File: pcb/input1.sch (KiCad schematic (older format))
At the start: 26 parts, among them U10 74LVC245, U11 SI5351C-B, U4 PCEngineExpansion, U5 74LVC245, U6 74LVC245, U7 74LVC245, U8 74LVC245, U9 74LVC245

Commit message: Added power unit from expansion connector symbol
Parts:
- removed W1: 5V, custom_components:SMD_PAD, symbol pcehd-rescue:TestPoint-Connector
- removed W2, W3, W4, W5, W6: GND, custom_components:SMD_PAD, symbol pcehd-rescue:TestPoint-Connector
- added unit 2 of U4
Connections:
- wire segments 232 -> 233
- no-connect marks 28 -> 32
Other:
- moved on the sheet: C27, C28, C29, C30, C31, C32, D4, R6, U11, U4A, U4F

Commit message: Cleaned up schematic, moved connections to busses
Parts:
- removed C27: 47u, custom_components:SM0603_Capa_libcms, symbol pcehd-rescue:C-Device
- removed D4: SD05-7, custom_components:SOD-323_Handsoldering, symbol pcehd-rescue:D_Zener_Small_ALT-Device
- removed unit 2 of U4
- removed unit 1 of U4
- added C86: 0.1u, custom_components:SM0603_Capa_libcms, symbol pcehd-rescue:C-Device
- added U18: SN74LVC2G17, MODULE, symbol custom_components:SN74LVC2G17
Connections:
- net labels added: A0, A1, A10, A11, A12, A13, A14, A15, A16, A17, A18, A19, A2, A20, A3, A4, A5, A6, A7, A8, A9, A[0..20], D0, D1, D2, D3, D4, D5, D6, D7, DCK, D[0..7], HSn_O, VD0, VD1, VD2, VD3, VD4, VD5, VD6, VD7, VD[0..7], VSn_O
- net labels removed: A0_O, A10_O, A11_O, A12_O, A16_O, A1_O, A20_O, A2_O, A3_O, A4_O, A5_O, A6_O, A7_O, A8_O, A9_O, AudioL_O, AudioR_O, D0_IO, D1_IO, D2_IO, D3_IO, D4_IO, D5_IO, D6_IO, D7_IO, DVDD5V, VD0_O, VD1_O, VD2_O, VD3_O, VD4_O, VD5_O, VD6_O, VD7_O
- wire segments 233 -> 234
- no-connect marks 32 -> 16
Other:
- moved on the sheet: C23, C24, C25, C26, C28, C29, C30, C31, C32, R6, U11, U4C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

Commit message: Added clock selection
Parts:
- added J2: Conn_Coaxial, Connector_Coaxial:SMA_Amphenol_132289_EdgeMount, symbol Connector:Conn_Coaxial
- added JP1, JP2: SolderJumper_2_Open, Jumper:SolderJumper-2_P1.3mm_Open_RoundedPad1.0x1.5mm, symbol Jumper:SolderJumper_2_Open
- added R17, R19: R_Small, custom_components:SM0603_Resistor_libcms, symbol Device:R_Small
- added U19: 74153, Package_SO:SOIC-16_3.9x9.9mm_P1.27mm, symbol 74xx_IEEE:74153
- added Y1: 25.000MHz, Crystal:Crystal_SMD_SeikoEpson_FA238-4Pin_3.2x2.5mm_HandSoldering, symbol Device:Crystal_GND24_Small
- U18: footprint MODULE -> custom_components:SOT-23-6_Handsoldering
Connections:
- net labels added: DCKFB_I, SI_CLK0_O, SI_CLK1_O
- net labels removed: DCK_SI
- wire segments 234 -> 262
- no-connect marks 16 -> 17
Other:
- moved on the sheet: C28, C29, C30, C31, C32, C86, R6, U11, U18, U4F

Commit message: Added FS7140 PLL, moved to level-shift '245
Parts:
- removed C24, C25, C26, C28, C29, C30, C31, C32: 0.1u, custom_components:SM0603_Capa_libcms, symbol pcehd-rescue:C-Device
- removed J2: Conn_Coaxial, Connector_Coaxial:SMA_Amphenol_132289_EdgeMount, symbol Connector:Conn_Coaxial
- removed JP1, JP2: SolderJumper_2_Open, Jumper:SolderJumper-2_P1.3mm_Open_RoundedPad1.0x1.5mm, symbol Jumper:SolderJumper_2_Open
- removed R17, R19: R_Small, custom_components:SM0603_Resistor_libcms, symbol Device:R_Small
- removed R6: 4.7k, custom_components:SM0603_Resistor_libcms, symbol pcehd-rescue:R-Device
- removed U10, U5, U6, U7, U8, U9: 74LVC245, custom_components:TSSOP-20_4.4x6.5mm_Pitch0.65mm_Handsoldering, symbol custom_components:74LVC245
- removed U11: SI5351C-B, custom_components:QFN-20-1EP_4x4mm_Pitch0.5mm_Handsoldering, symbol custom_components:Si5351C
- removed U18: SN74LVC2G17, custom_components:SOT-23-6_Handsoldering, symbol custom_components:SN74LVC2G17
- removed U19: 74153, Package_SO:SOIC-16_3.9x9.9mm_P1.27mm, symbol 74xx_IEEE:74153
- removed Y1: 25.000MHz, Crystal:Crystal_SMD_SeikoEpson_FA238-4Pin_3.2x2.5mm_HandSoldering, symbol Device:Crystal_GND24_Small
- added C81, C82, C83, C84, C85, C87, C88, C89, C90: 0.1u, custom_components:SM0603_Capa_libcms, symbol pcehd-rescue:C-Device
- added Q1, Q2: BC847, Package_TO_SOT_SMD:SOT-23, symbol Transistor_BJT:BC847
- added R22, R24: 1K, custom_components:SM0603_Resistor_libcms, symbol Device:R_Small
- added R23, R25, R26, R27, R28, R29: 10K, custom_components:SM0603_Resistor_libcms, symbol Device:R_Small
- added U10, U11, U14, U18, U9: SN74LVCC4245APW, custom_components:SN74LVCC4245APW, symbol custom_components:SN74LVCC4245APW
- added U19: SN74LVC3G17, MODULE, symbol custom_components:SN74LVC3G17
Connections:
- net labels added: 5V, CEK, HSn, SPBG
- net labels removed: CDD, DCK, DCKFB_I, RST_N, SCL, SDA, SI_CLK0_O, SI_CLK1_O, VSn_O, XRD_O
- wire segments 262 -> 250
- no-connect marks 17 -> 7
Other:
- moved on the sheet: C23, U4C, U4D, U4E, U4F

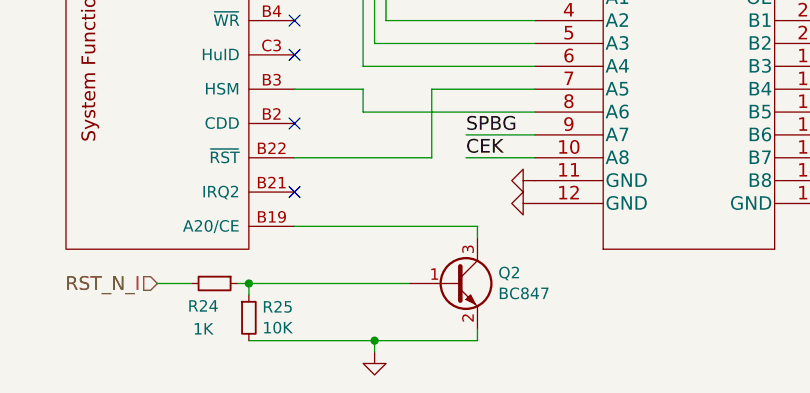
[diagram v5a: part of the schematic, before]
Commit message: Assigned footprints, begin layout
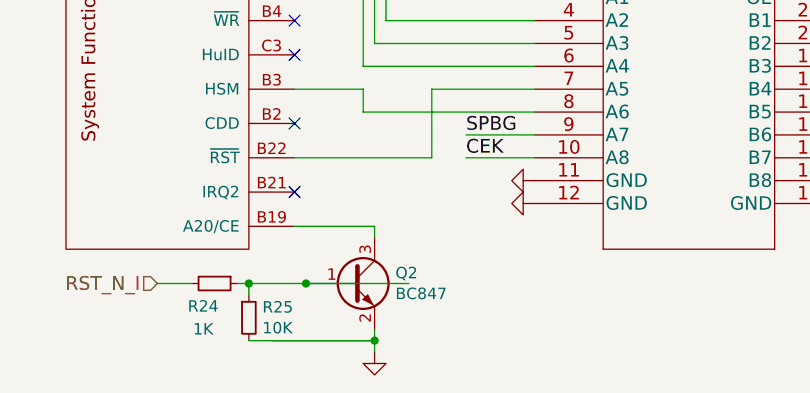
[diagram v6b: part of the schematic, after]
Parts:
- U19: footprint MODULE -> custom_components:SSOP-8_3x3mm_Pitch0.65mm
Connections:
- wire segments 250 -> 251
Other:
- moved on the sheet: Q2
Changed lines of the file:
@@
 	1100 4900 1200 4900
 Wire Wire Line
-	2800 6950 2800 7000
-Wire Wire Line
-	2000 6950 2800 6950
+	2350 6950 2350 7000
 Wire Wire Line
 	1800 7250 1800 7200
@@
 Connection ~ 1800 7200
 Wire Wire Line
-	1800 7200 2500 7200
-Wire Wire Line
-	1800 7450 2350 7450
+	1800 7200 2050 7200
 Wire Wire Line
 	2350 7450 2350 7500
 Wire Wire Line
-	2350 7450 2800 7450
-Wire Wire Line
-	2800 7450 2800 7400
+	2350 7450 2350 7400
 Connection ~ 2350 7450
 $Comp
 L Transistor_BJT:BC847 Q2
 U 1 1 60FF82DE
-P 2700 7200
-F 0 "Q2" H 2891 7246 50  0000 L CNN
-F 1 "BC847" H 2891 7155 50  0000 L CNN
-F 2 "Package_TO_SOT_SMD:SOT-23" H 2900 7125 50  0001 L CIN
-F 3 "http://www.infineon.com/dgdl/Infineon-BC847SERIES_BC848SERIES_BC849SERIES_BC850SERIES-DS-v01_01-en.pdf?fileId=db3a304314dca389011541d4630a1657" H 2700 7200 50  0001 L CNN
-	1    2700 7200
+P 2250 7200
+F 0 "Q2" H 2441 7246 50  0000 L CNN
+F 1 "BC847" H 2441 7155 50  0000 L CNN
+F 2 "Package_TO_SOT_SMD:SOT-23" H 2450 7125 50  0001 L CIN
+F 3 "http://www.infineon.com/dgdl/Infineon-BC847SERIES_BC848SERIES_BC849SERIES_BC850SERIES-DS-v01_01-en.pdf?fileId=db3a304314dca389011541d4630a1657" H 2250 7200 50  0001 L CNN
+	1    2250 7200
 	1    0    0    -1
 $EndComp
@@
 F 0 "U19" H 8500 4415 50  0000 C CNN
 F 1 "SN74LVC3G17" H 8500 4324 50  0000 C CNN
-F 2 "MODULE" H 8500 3900 50  0001 C CNN
+F 2 "custom_components:SSOP-8_3x3mm_Pitch0.65mm" H 8500 3900 50  0001 C CNN
 F 3 "DOCUMENTATION" H 8500 3650 50  0001 C CNN
 	1    8500 3900
@@
 Text Label 3050 3300 1    60   ~ 0
 5V
+Wire Wire Line
+	2000 6950 2350 6950
+Connection ~ 2050 7200
+Wire Wire Line
+	2050 7200 2500 7200
+Wire Wire Line
+	1900 7450 2350 7450
+Wire Wire Line
+	1800 7450 2350 7450
 Wire Bus Line
 	9550 5600 9550 6550

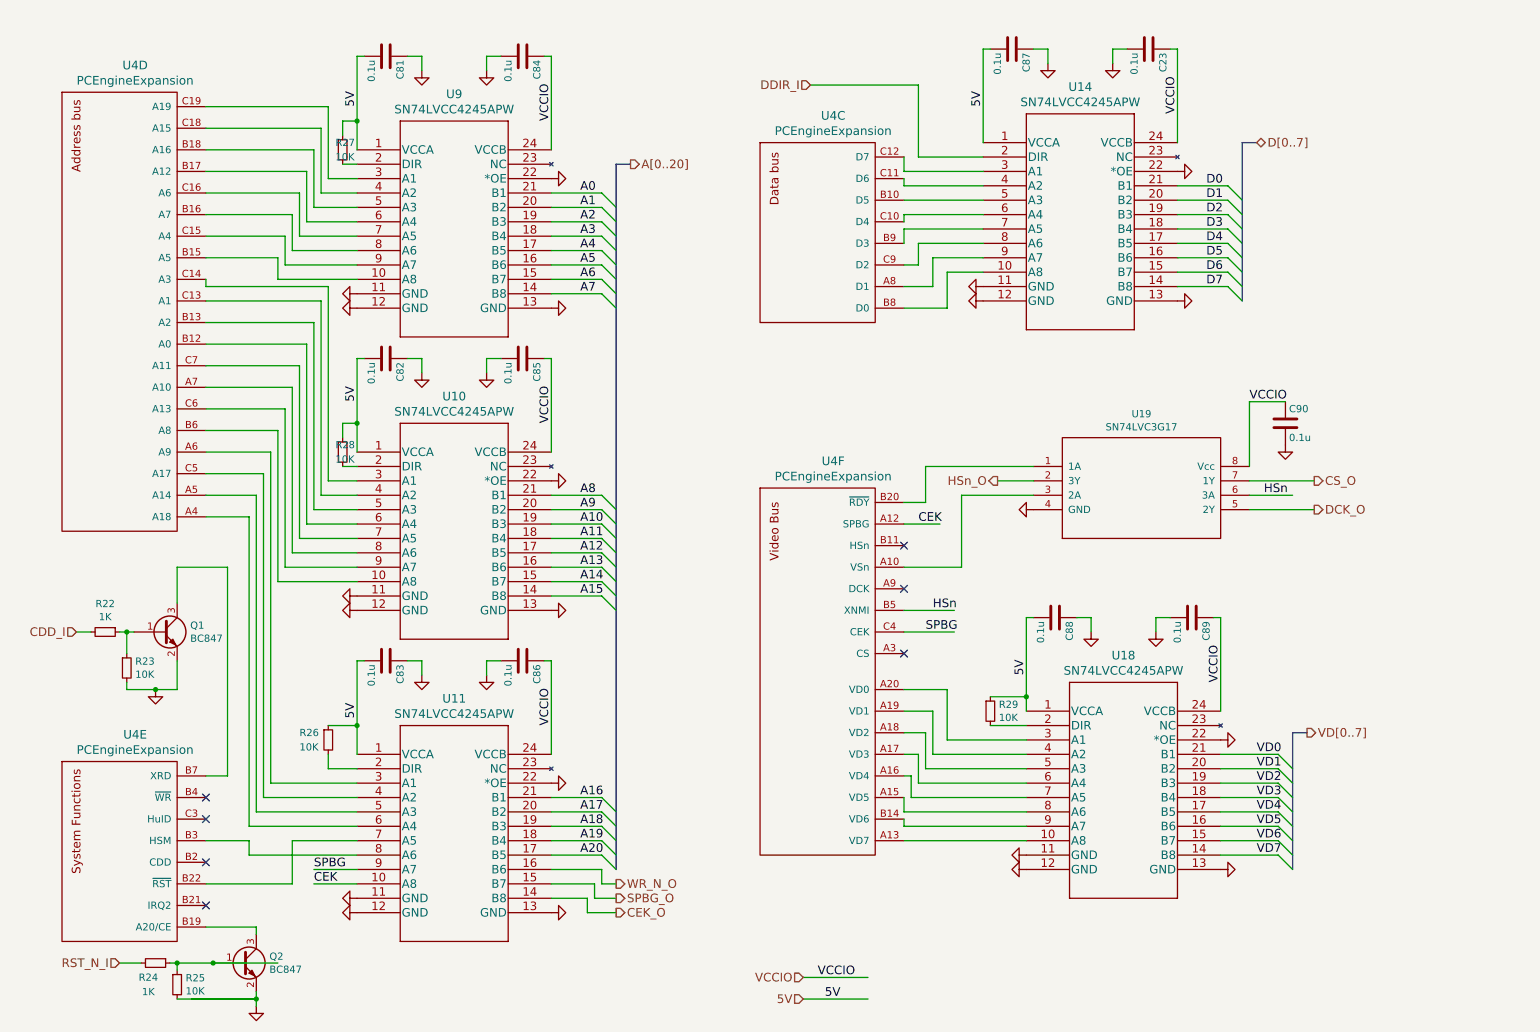
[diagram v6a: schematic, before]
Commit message: Expansion connection re-order for layout
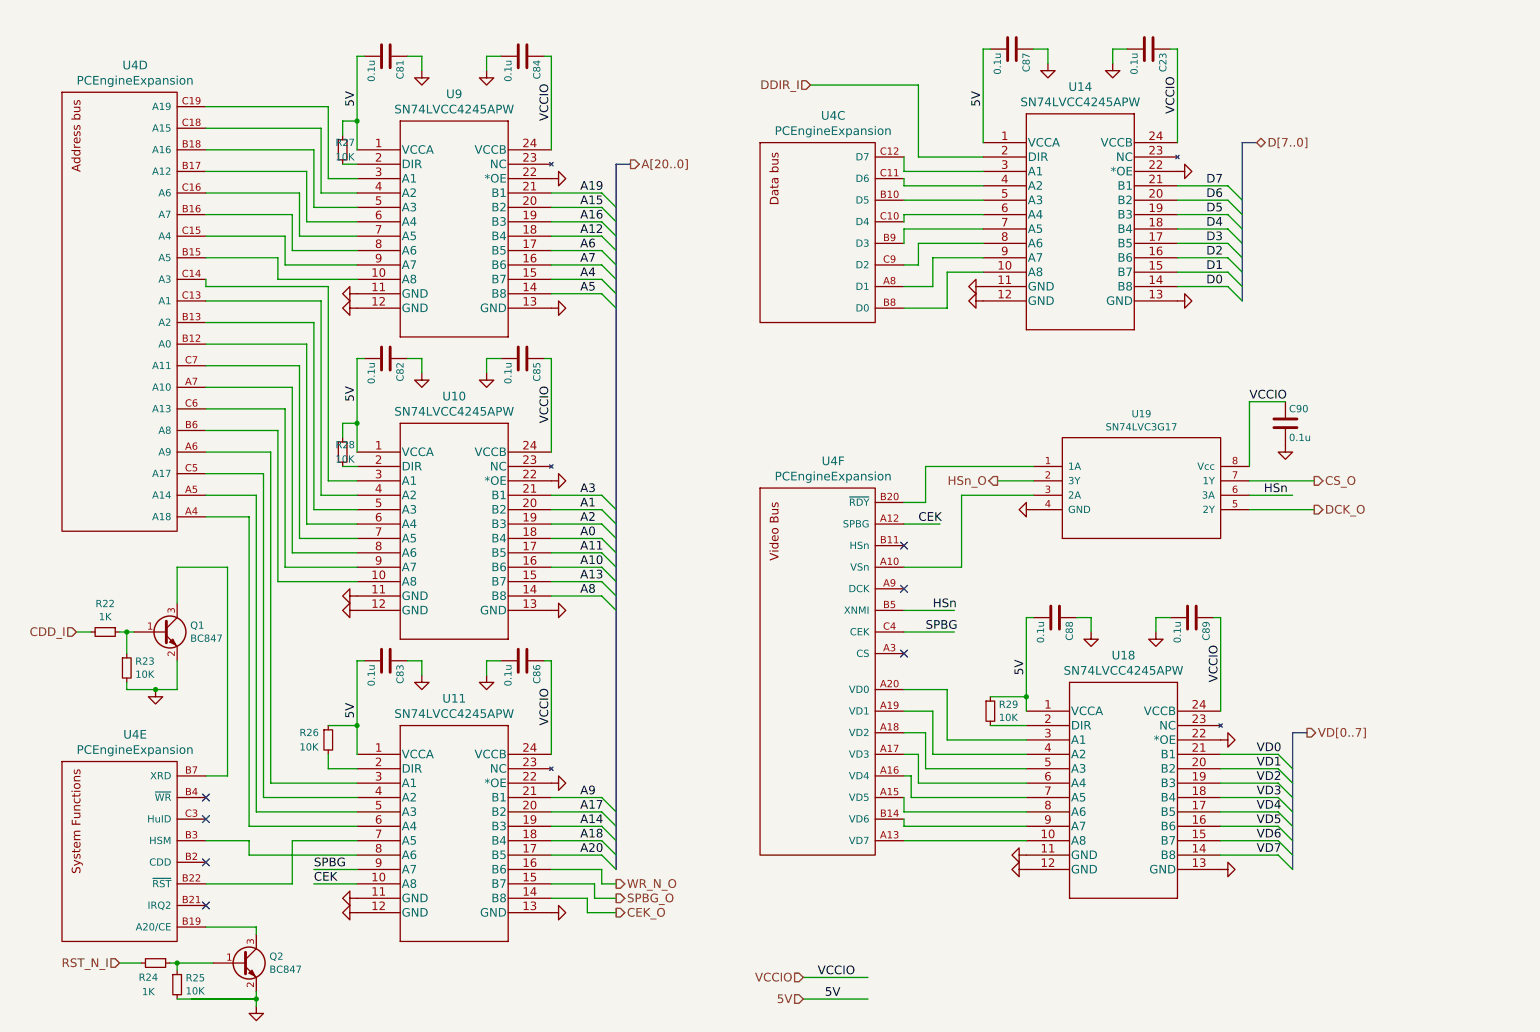
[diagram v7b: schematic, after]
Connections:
- net labels added: A[20..0], D[7..0]
- net labels removed: A[0..20], D[0..7]
- wire segments 251 -> 250
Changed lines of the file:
@@
 CEK_O
 Text HLabel 9300 1500 2    60   BiDi ~ 0
-D[0..7]
+D[7..0]
 Entry Wire Line
 	9100 2500 9200 2600
@@
 	9100 1800 9200 1900
 Text Label 8950 1800 0    60   ~ 0
+D7
+Text Label 8950 1900 0    60   ~ 0
+D6
+Text Label 8950 2000 0    60   ~ 0
+D5
+Text Label 8950 2100 0    60   ~ 0
+D4
+Text Label 8950 2200 0    60   ~ 0
+D3
+Text Label 8950 2300 0    60   ~ 0
+D2
+Text Label 8950 2400 0    60   ~ 0
+D1
+Text Label 8950 2500 0    60   ~ 0
 D0
-Text Label 8950 1900 0    60   ~ 0
-D1
-Text Label 8950 2000 0    60   ~ 0
-D2
-Text Label 8950 2100 0    60   ~ 0
-D3
-Text Label 8950 2200 0    60   ~ 0
-D4
-Text Label 8950 2300 0    60   ~ 0
-D5
-Text Label 8950 2400 0    60   ~ 0
-D6
-Text Label 8950 2500 0    60   ~ 0
-D7
 Entry Wire Line
 	4750 4650 4850 4750
@@
 	4750 1850 4850 1950
 Text Label 4600 1850 0    60   ~ 0
-A0
+A19
 Text Label 4600 1950 0    60   ~ 0
-A1
+A15
 Text Label 4600 2050 0    60   ~ 0
-A2
+A16
 Text Label 4600 2150 0    60   ~ 0
-A3
+A12
 Text Label 4600 2250 0    60   ~ 0
+A6
+Text Label 4600 2350 0    60   ~ 0
+A7
+Text Label 4600 2450 0    60   ~ 0
 A4
-Text Label 4600 2350 0    60   ~ 0
+Text Label 4600 2550 0    60   ~ 0
 A5
-Text Label 4600 2450 0    60   ~ 0
-A6
-Text Label 4600 2550 0    60   ~ 0
-A7
 Text HLabel 4850 6650 2    60   Output ~ 0
 WR_N_O
@@
 	4750 6350 4850 6450
 Text Label 4600 6050 0    60   ~ 0
-A16
+A9
 Text Label 4600 6150 0    60   ~ 0
 A17
 Text Label 4600 6250 0    60   ~ 0
+A14
+Text Label 4600 6350 0    60   ~ 0
 A18
-Text Label 4600 6350 0    60   ~ 0
-A19
 Entry Wire Line
 	4750 6450 4850 6550
@@
 A20
 Text HLabel 4950 1650 2    60   Output ~ 0
-A[0..20]
+A[20..0]
 Wire Bus Line
 	4950 1650 4850 1650
@@
 	4400 2550 4750 2550
 Text Label 4600 4650 0    60   ~ 0
-A15
+A8
 Text Label 4600 4550 0    60   ~ 0
-A14
+A13
 Text Label 4600 4450 0    60   ~ 0
-A13
+A10
 Text Label 4600 4350 0    60   ~ 0
-A12
+A11
 Text Label 4600 4250 0    60   ~ 0
-A11
+A0
 Text Label 4600 4150 0    60   ~ 0
-A10
+A2
 Text Label 4600 4050 0    60   ~ 0
-A9
+A1
 Text Label 4600 3950 0    60   ~ 0
-A8
+A3
 Wire Wire Line
 	4400 3950 4750 3950
@@
 Wire Wire Line
 	1750 7200 1800 7200
-Connection ~ 1800 7200
-Wire Wire Line
-	1800 7200 2050 7200
 Wire Wire Line
 	2350 7450 2350 7500
@@
 Wire Wire Line
 	2000 6950 2350 6950
-Connection ~ 2050 7200
-Wire Wire Line
-	2050 7200 2500 7200
 Wire Wire Line
 	1900 7450 2350 7450
 Wire Wire Line
 	1800 7450 2350 7450
+Wire Wire Line
+	1800 7200 2050 7200
+Connection ~ 1800 7200
 Wire Bus Line
 	9550 5600 9550 6550

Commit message: New layout
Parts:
- removed U19: SN74LVC3G17, custom_components:SSOP-8_3x3mm_Pitch0.65mm, symbol custom_components:SN74LVC3G17
- added C91, C92: 0.1u, custom_components:SM0603_Capa_libcms, symbol pcehd-rescue:C-Device
- added R30: 10K, custom_components:SM0603_Resistor_libcms, symbol Device:R_Small
- added U19: SN74LVCC4245APW, custom_components:SN74LVCC4245APW, symbol custom_components:SN74LVCC4245APW
- added U20: SN74LVC2G17, custom_components:SOT-23-6_Handsoldering, symbol custom_components:SN74LVC2G17
- R22: value 1K -> 10K
- R23: value 10K -> 1K
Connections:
- net labels added: CS, DCK, HuID, HuID_N_I, HuID_N_O, RDYn, RSTn, VSn, WRn, XNMI, XRD, XRD_O
- net labels removed: CDD_I
- wire segments 250 -> 255
- no-connect marks 7 -> 8
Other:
- moved on the sheet: C23, C81, C82, C83, C84, C85, C86, C87, C88, C89, C90, Q2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
